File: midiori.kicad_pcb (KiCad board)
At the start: 2 copper layers, 46 parts, among them J1 x68000_expansion, U1 74LS245, U10 74LS393, U11 74LS74, U12 74LS04, U13 H11L1, U14 7407, U15 74LS157, U2 74LS133, U3 74LS133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

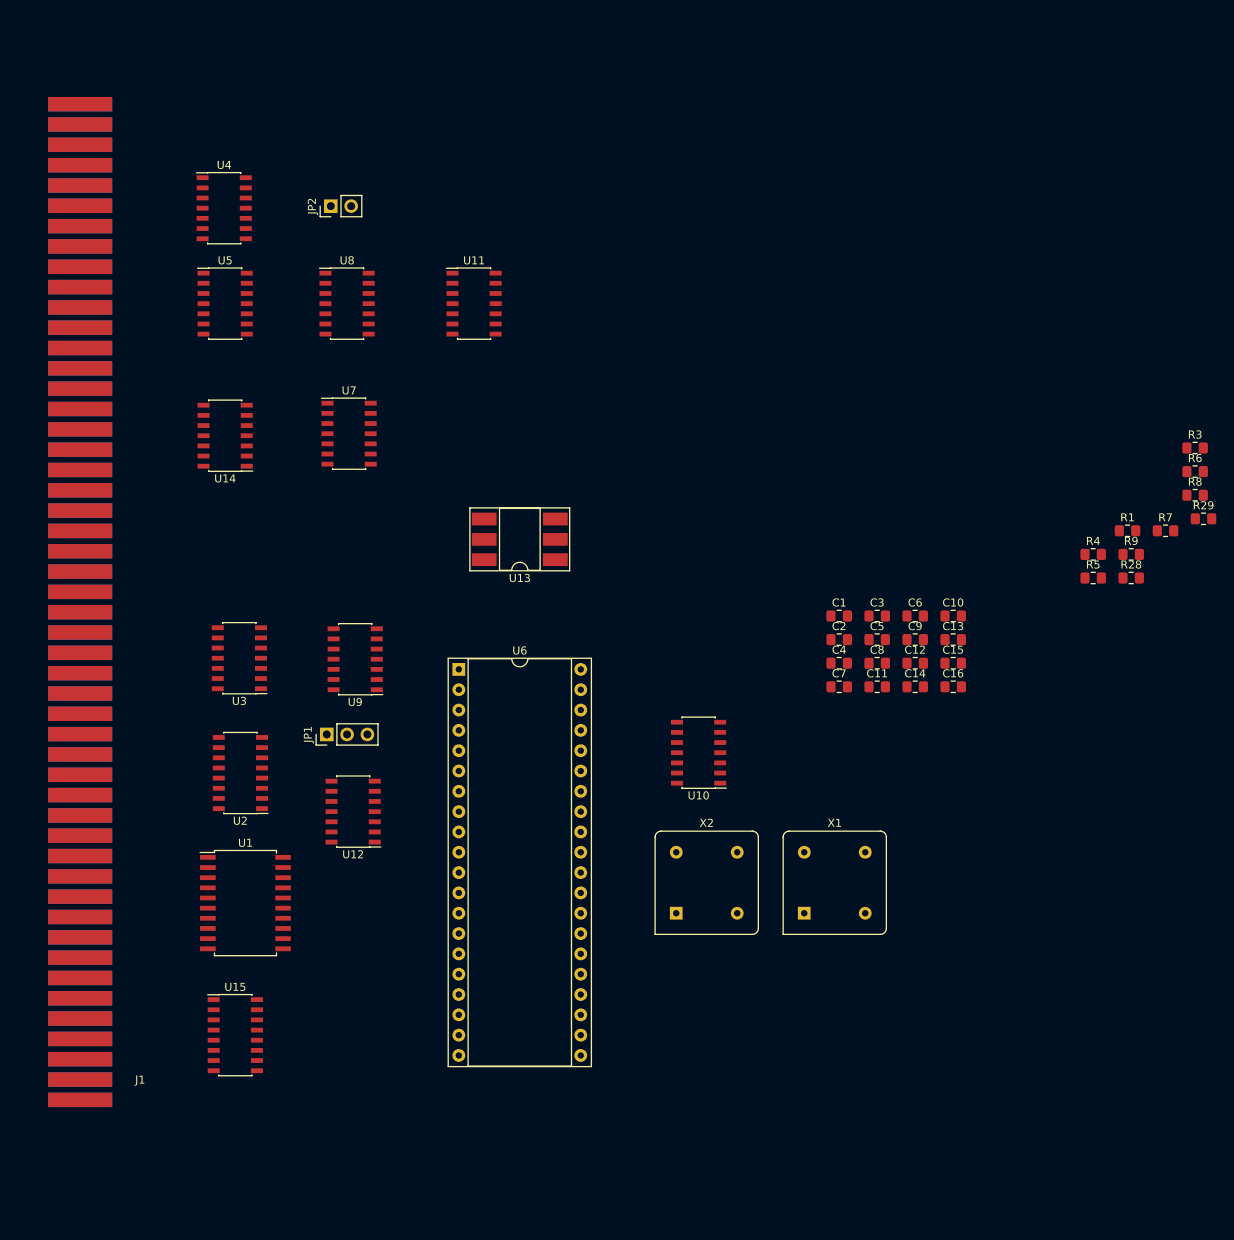
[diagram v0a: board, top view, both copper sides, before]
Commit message: Add board outline
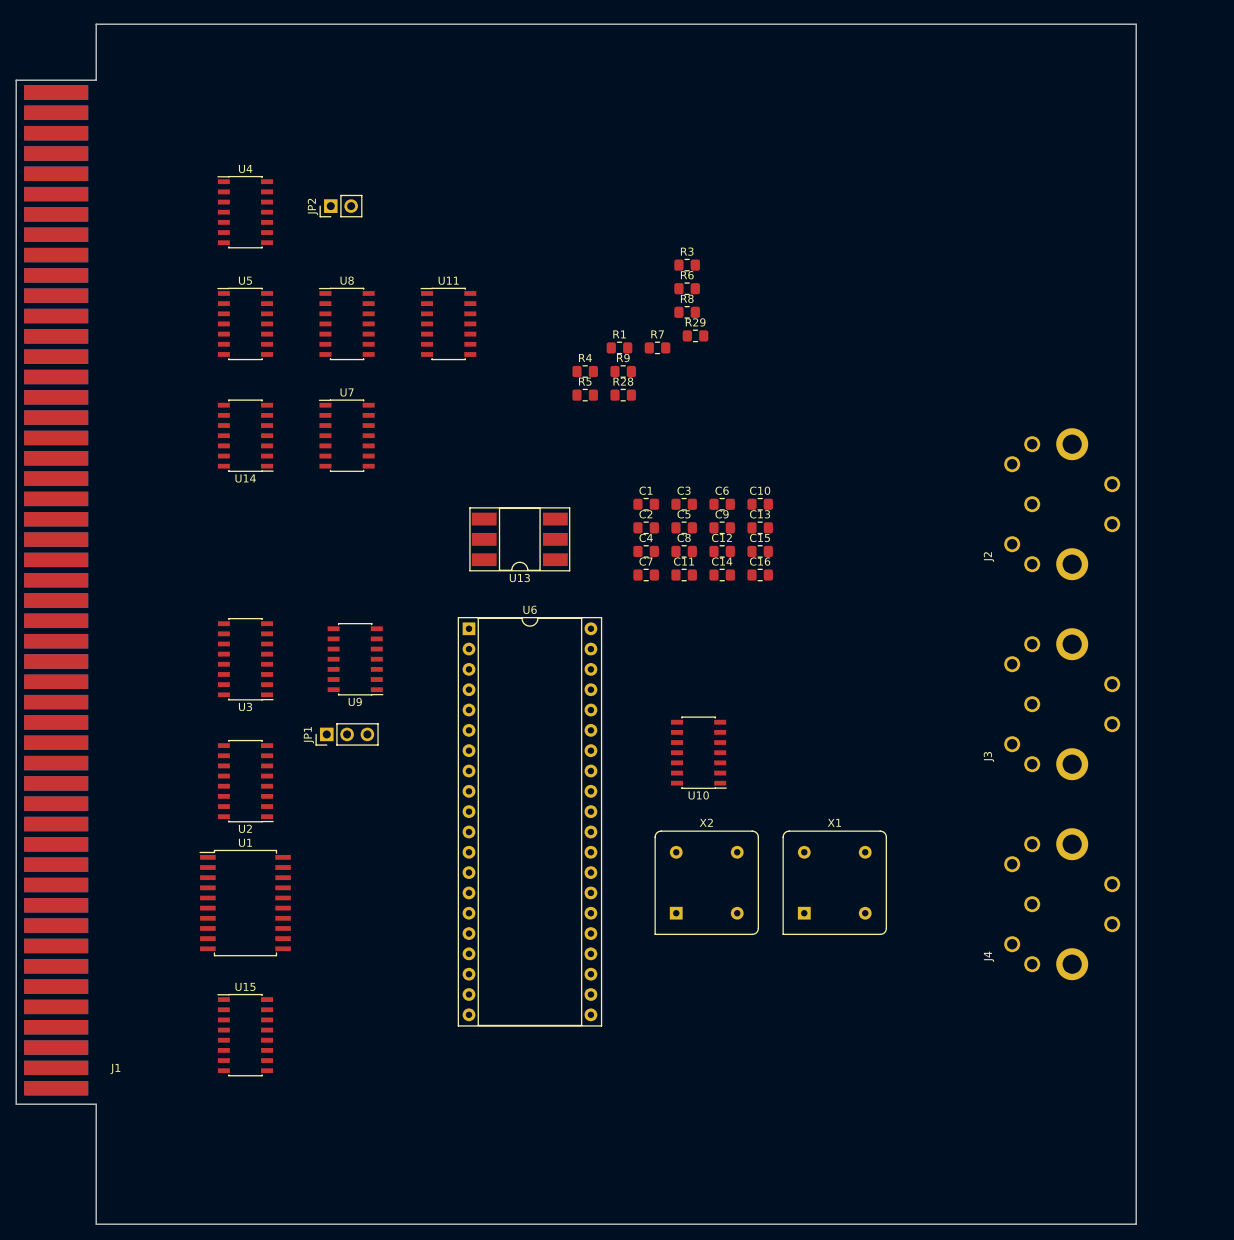
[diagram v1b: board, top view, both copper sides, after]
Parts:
- removed U12: 74LS04, Package_SO:SOIC-14_3.9x8.7mm_P1.27mm
- added J2: DIN-5_180degree, x68k:sds-50j, F.Cu at (172.0, 100.0)
- added J3: DIN-5_180degree, x68k:sds-50j, F.Cu at (172.0, 125.0)
- added J4: DIN-5_180degree, x68k:sds-50j, F.Cu at (172.0, 150.0)
- U3: footprint Package_SO:SOIC-14_3.9x8.7mm_P1.27mm -> Package_SO:SOIC-16_3.9x9.9mm_P1.27mm
- moved R28 67.5 mm to (120.9, 86.4)
- moved R29 67.5 mm to (129.9, 79.0)
- moved R3 67.5 mm to (128.9, 70.1)
- moved R4 67.5 mm to (116.1, 83.4)
- moved R5 67.5 mm to (116.1, 86.4)
- moved R6 67.5 mm to (128.9, 73.1)
- moved R8 67.5 mm to (128.9, 76.0)
- moved R9 67.5 mm to (120.9, 83.4)
- moved R1 67.5 mm to (120.4, 80.5)
- moved R7 67.5 mm to (125.2, 80.5)
- moved C1 27.9 mm to (123.7, 100.0)
- moved C10 27.9 mm to (138.0, 100.0)
- moved C3 27.9 mm to (128.5, 100.0)
- moved C6 27.9 mm to (133.2, 100.0)
- moved C11 27.9 mm to (128.5, 108.9)
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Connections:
- U8 pad 10: (no net) -> Net-(JP1-Pad3)
- U8 pad 11: (no net) -> /AB4
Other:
- board outline added: 140 x 150 mm

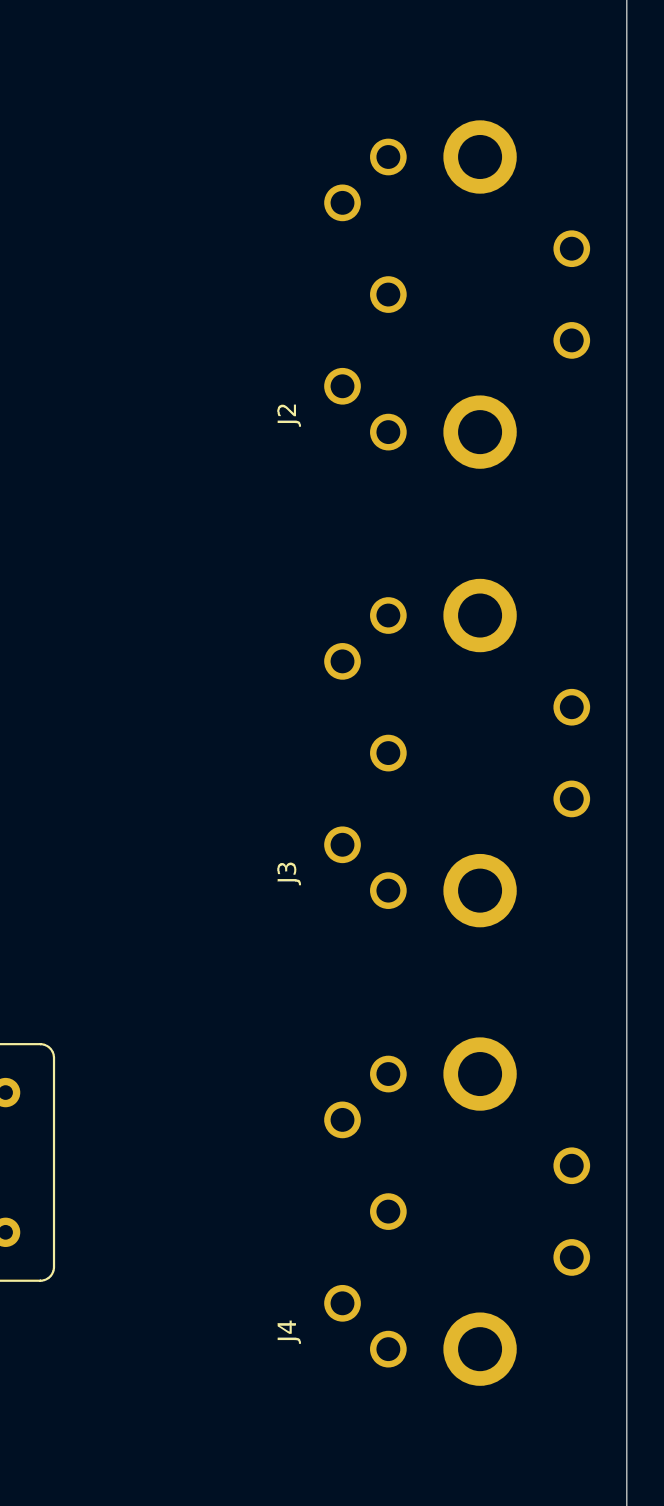
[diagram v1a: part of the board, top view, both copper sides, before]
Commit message: Remove 74ls133 from address decoding
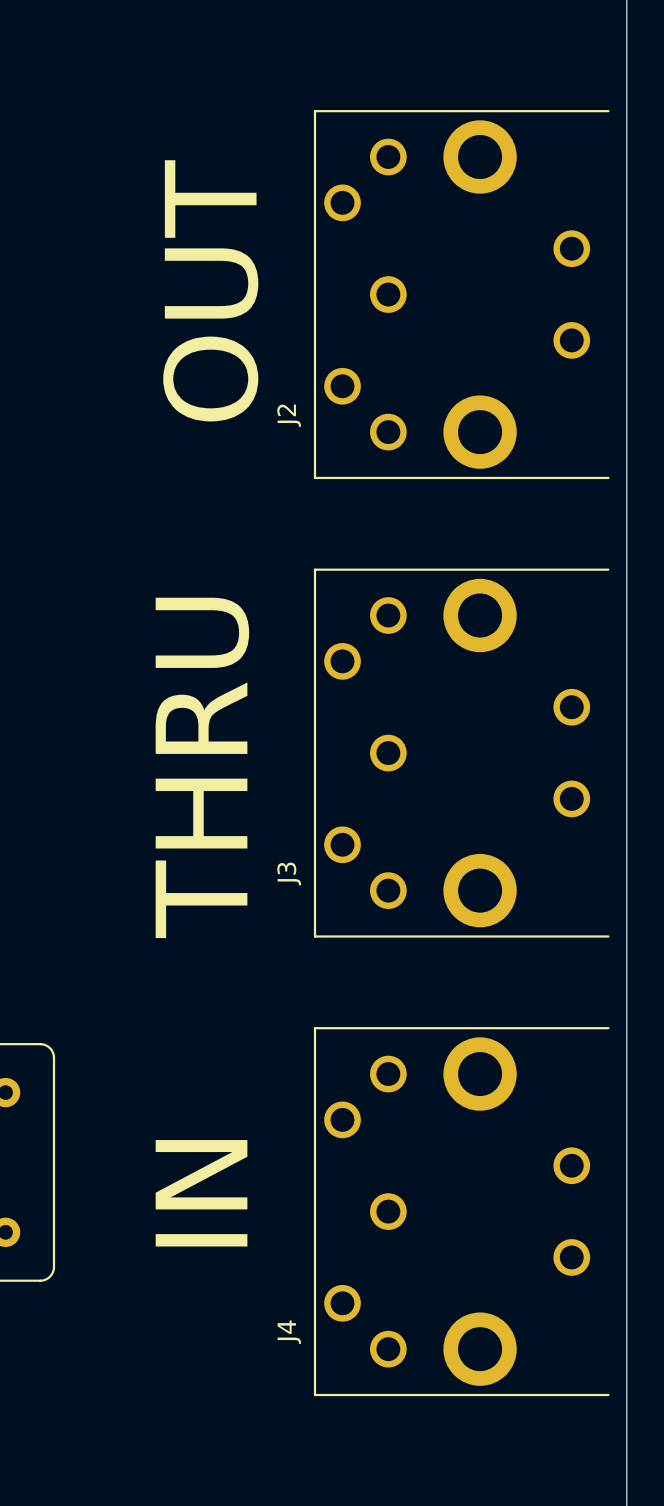
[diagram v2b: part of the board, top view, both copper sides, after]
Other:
- board text added: "IN"
- board text added: "OUT"
- board text added: "THRU"
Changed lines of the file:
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@@
   (general
     (thickness 1.6)
-    (drawings 8)
+    (drawings 11)
     (tracks 0)
     (zones 0)
@@
       (effects (font (size 1 1) (thickness 0.15)))
     )
+    (fp_line (start 10 -4) (end 10 12) (layer F.SilkS) (width 0.12))
+    (fp_line (start -10 -4) (end 10 -4) (layer F.SilkS) (width 0.12))
+    (fp_line (start -10 12) (end -10 -4) (layer F.SilkS) (width 0.12))
     (fp_line (start 10 -4) (end 10 12.5) (layer F.CrtYd) (width 0.12))
     (fp_line (start -10 -4) (end 10 -4) (layer F.CrtYd) (width 0.12))
@@
       (effects (font (size 1 1) (thickness 0.15)))
     )
+    (fp_line (start 10 -4) (end 10 12) (layer F.SilkS) (width 0.12))
+    (fp_line (start -10 -4) (end 10 -4) (layer F.SilkS) (width 0.12))
+    (fp_line (start -10 12) (end -10 -4) (layer F.SilkS) (width 0.12))
     (fp_line (start 10 -4) (end 10 12.5) (layer F.CrtYd) (width 0.12))
     (fp_line (start -10 -4) (end 10 -4) (layer F.CrtYd) (width 0.12))
@@
       (effects (font (size 1 1) (thickness 0.15)))
     )
+    (fp_line (start 10 -4) (end 10 12) (layer F.SilkS) (width 0.12))
+    (fp_line (start -10 -4) (end 10 -4) (layer F.SilkS) (width 0.12))
+    (fp_line (start -10 12) (end -10 -4) (layer F.SilkS) (width 0.12))
     (fp_line (start 10 -4) (end 10 12.5) (layer F.CrtYd) (width 0.12))
     (fp_line (start -10 -4) (end 10 -4) (layer F.CrtYd) (width 0.12))
@@
     )
   )
+  (gr_text OUT (at 162.5 100 90) (layer F.SilkS)
+    (effects (font (size 5 5) (thickness 0.15)))
+  )
+  (gr_text THRU (at 162 125.5 90) (layer F.SilkS)
+    (effects (font (size 5 5) (thickness 0.15)))
+  )
+  (gr_text IN (at 162 149 90) (layer F.SilkS)
+    (effects (font (size 5 5) (thickness 0.15)))
+  )
   (gr_line (start 55 47) (end 45 47) (layer Edge.Cuts) (width 0.05))

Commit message: more
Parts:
- removed C15, C2: u1, Capacitor_SMD:C_0805_2012Metric_Pad1.15x1.40mm_HandSolder
- added C17: u1, Capacitor_SMD:C_0805_2012Metric_Pad1.15x1.40mm_HandSolder, F.Cu at (130.8, 137.2)
- added REF**: MountingHole_3.2mm_M3_Pad, MountingHole:MountingHole_3.2mm_M3_Pad, F.Cu at (181.0, 56.0)
- added REF**: MountingHole_3.2mm_M3_Pad, MountingHole:MountingHole_3.2mm_M3_Pad, F.Cu at (181.0, 46.0)
- added REF**: MountingHole_3.2mm_M3_Pad, MountingHole:MountingHole_3.2mm_M3_Pad, F.Cu at (181.0, 174.0)
- added REF**: MountingHole_3.2mm_M3_Pad, MountingHole:MountingHole_3.2mm_M3_Pad, F.Cu at (181.0, 184.0)
- added U12: 74LS30, Package_SO:SOIC-14_3.9x8.7mm_P1.27mm, F.Cu at (73.7, 121.9)
- U14: value 7407 -> 74LS07
- U2: value 74LS133 -> 74LS27; footprint Package_SO:SOIC-16_3.9x9.9mm_P1.27mm -> Package_SO:SOIC-14_3.9x8.7mm_P1.27mm
- U3: value 74LS133 -> 74LS30; footprint Package_SO:SOIC-16_3.9x9.9mm_P1.27mm -> Package_SO:SOIC-14_3.9x8.7mm_P1.27mm
- X1: value CXO_DIP8 -> 16MHz; footprint Oscillator:Oscillator_DIP-8 -> Oscillator:Oscillator_SMD_SeikoEpson_SG8002CA-4Pin_7.0x5.0mm
- X2: value CXO_DIP8 -> 4.9152MHz; footprint Oscillator:Oscillator_DIP-8 -> Oscillator:Oscillator_SMD_SeikoEpson_SG8002CA-4Pin_7.0x5.0mm
- moved C7 82.2 mm to (73.7, 174.0), turned to 180 degrees
- moved C11 74.0 mm to (73.9, 158.8), turned to 180 degrees
- moved C9 67.9 mm to (73.9, 69.8), turned to 180 degrees
- moved R8 63.7 mm to (153.9, 134.6), turned to 180 degrees
- moved C6 61.5 mm to (73.9, 83.8)
- moved C4 60.9 mm to (73.9, 141.0)
- moved C10 58.7 mm to (86.6, 128.3)
- moved C1 57.3 mm to (73.9, 128.3), turned to 180 degrees
- moved C16 57.2 mm to (86.6, 83.8), turned to 180 degrees
- moved C5 55.6 mm to (73.9, 113.5)
- moved R7 54.7 mm to (153.9, 127.0)
- moved C3 54.6 mm to (73.9, 97.8)
- moved R9 50.7 mm to (153.9, 121.9), turned to 180 degrees
- moved R6 50.4 mm to (153.9, 116.8)
- moved R3 45.1 mm to (85.3, 58.4)
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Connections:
- U2 pad 10: GND -> /AB20
- U2 pad 11: GND -> /AB10
- U2 pad 12: /AB18 -> Net-(U2-Pad12)
- U2 pad 13: /AB16 -> Net-(JP1-Pad2)
- U2 pad 14: /AB20 -> +5V
- U2 pad 3: Net-(JP1-Pad2) -> /AB7
- U2 pad 5: /AB7 -> /AB18
- U2 pad 6: GND -> Net-(U2-Pad6)
- U2 pad 8: GND -> Net-(U2-Pad8)
- U2 pad 9: Net-(U2-Pad9) -> /AB16
- U3 pad 1: Net-(U2-Pad9) -> Net-(U2-Pad12)
- U3 pad 10: /AB15 -> (no net)
- U3 pad 11: /AB14 -> /AB17
- U3 pad 12: /AB13 -> Net-(U3-Pad12)
- U3 pad 13: /AB12 -> (no net)
- U3 pad 14: /AB11 -> (no net)
- U3 pad 2: +5V -> Net-(U2-Pad6)
- U3 pad 3: /AB21 -> Net-(U2-Pad8)
- U3 pad 4: /AB22 -> /AB21
- U3 pad 5: /AB19 -> /AB22
- U3 pad 6: /AB17 -> /AB19
- U3 pad 7: Net-(U3-Pad7) -> (no net)
- U3 pad 8: GND -> Net-(U3-Pad8)
- U3 pad 9: Net-(U3-Pad9) -> (no net)
- U4 pad 10: Net-(U3-Pad9) -> Net-(U3-Pad8)
- U4 pad 11: (no net) -> Net-(U4-Pad11)
- U4 pad 12: (no net) -> Net-(U12-Pad8)
- U4 pad 13: (no net) -> Net-(U4-Pad13)
- U4 pad 3: Net-(U3-Pad7) -> Net-(U3-Pad12)
- U4 pad 6: Net-(U4-Pad6) -> Net-(U4-Pad13)
- U4 pad 9: Net-(U4-Pad6) -> Net-(U4-Pad11)
- X1 pad 4: GND -> +5V
- X2 pad 4: GND -> +5V
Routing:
- net GND: track 0.00 -> 170.6 mm, vias 0 -> 27
- net /10MHz: track 0.00 -> 135.9 mm, vias 0 -> 1
- net /AB4: track 0.00 -> 106.4 mm, vias 0 -> 1
- net /A: track 0.00 -> 100.7 mm, vias 0 -> 3
- net Net-(R9-Pad2): track 0.00 -> 96.5 mm, vias 0 -> 2
- net Net-(R28-Pad2): track 0.00 -> 94.6 mm, vias 0 -> 1
- net Net-(R8-Pad2): track 0.00 -> 93.4 mm
- net Net-(U6-Pad32): track 0.00 -> 87.0 mm, vias 0 -> 4
- net Net-(R1-Pad2): track 0.00 -> 80.5 mm, vias 0 -> 2
- net /4MHz: track 0.00 -> 76.9 mm, vias 0 -> 1
- net Net-(U15-Pad7): track 0.00 -> 74.3 mm, vias 0 -> 1
- net Net-(R4-Pad2): track 0.00 -> 72.9 mm, vias 0 -> 2
- net Net-(U15-Pad4): track 0.00 -> 72.4 mm, vias 0 -> 1
- net Net-(U15-Pad9): track 0.00 -> 69.1 mm, vias 0 -> 1
- net Net-(U1-Pad19): track 0.00 -> 68.2 mm, vias 0 -> 2
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- added copper zone on F.Cu, net +5V
- added copper zone on B.Cu, net GND
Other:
- net class Default: clearance 0.2 -> 0.16; trace_width 0.25 -> 0.2; via_dia 0.8 -> 0.7
- rule trace_clearance: 0.2 -> 0.16
- board text added: "Address 1-2: 2-3:"
- board text added: "MIDIORI"
- board text added: "Short IRQ4 Open IRQ2"

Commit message: silkscreen improvements
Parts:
- added REF**: OSHW-Logo2_7.3x6mm_SilkScreen, Symbol:OSHW-Logo2_7.3x6mm_SilkScreen, F.Cu at (123.7, 69.8)
- added svg2mod: G***, x68k:midiori_logo, F.Cu at (138.2, 55.9)
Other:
- board text added: "1.0 2018 CC0 TD-Linux https://github.com/tdaede/midiori"
- board text added: "Address 1-2: EAFA00 2-3: EAFA10"
- board text removed: "Address 1-2: 2-3:"
- board text removed: "MIDIORI"
